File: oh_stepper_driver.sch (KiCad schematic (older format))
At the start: 19 parts, among them P2 CONN_01X02, P3 CONN_01X02, U2 STM32F446RCTx, X1 ABM8G

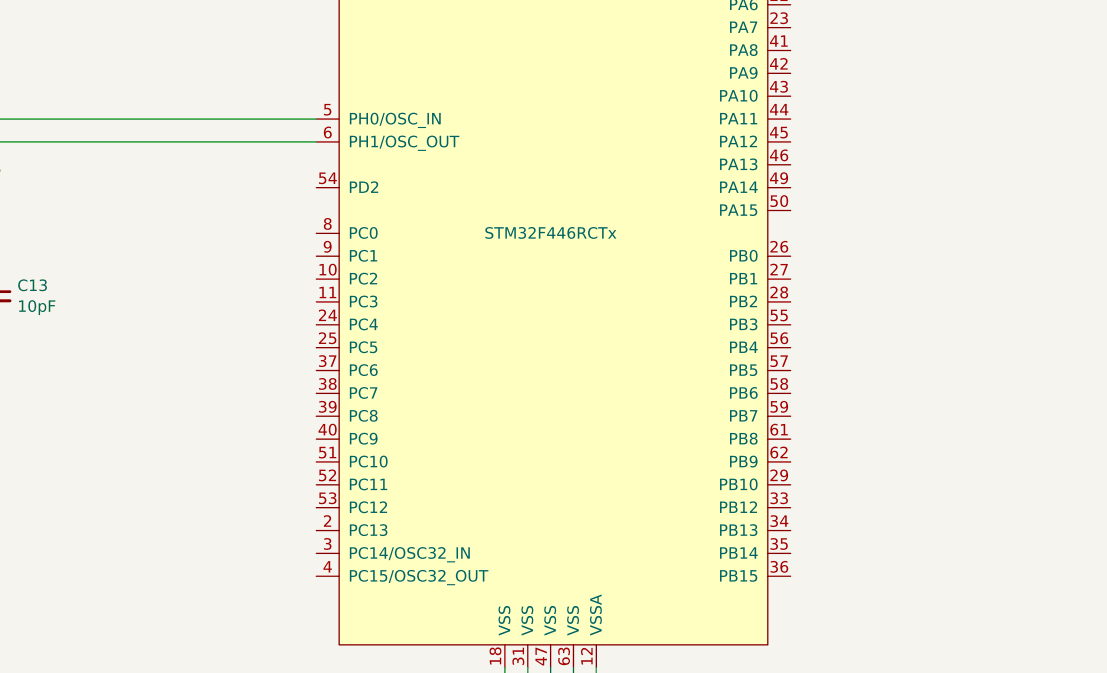
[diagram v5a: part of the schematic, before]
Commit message: connecting control lines between the motor driver and the STM32
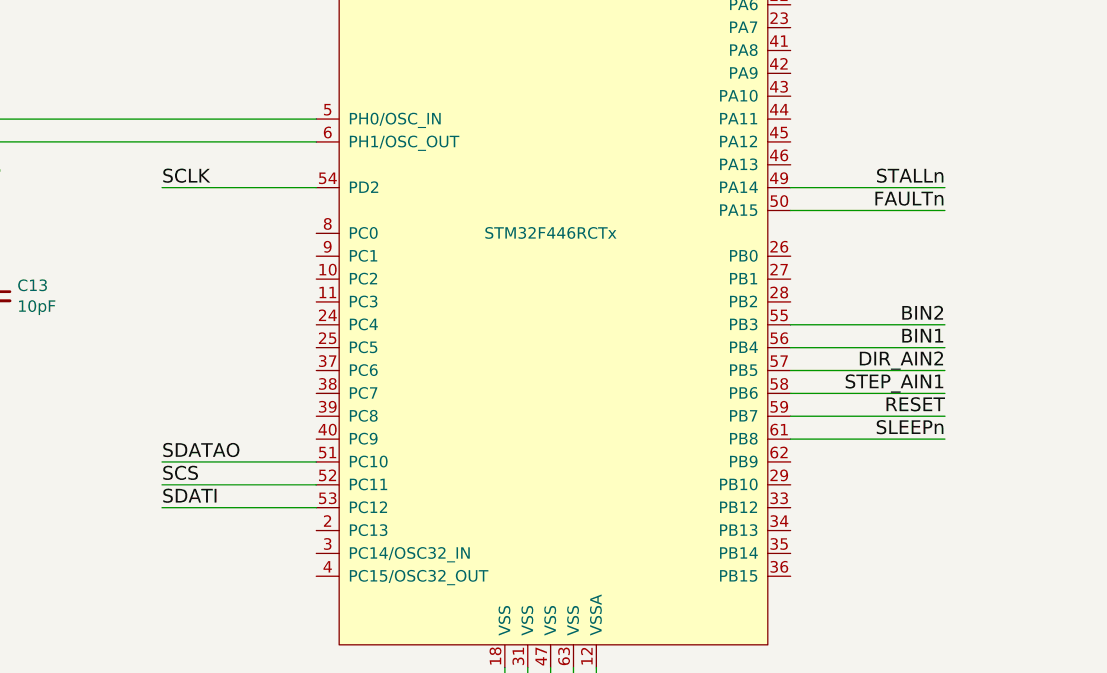
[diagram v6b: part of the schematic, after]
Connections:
- net BIN1: now also U2.56 (PB4)
- net BIN2: now also U2.55 (PB3)
- net DIR_AIN2: now also U2.57 (PB5)
- net FAULTn: now also U2.50 (PA15)
- net RESET: now also U2.59 (PB7)
- net SCLK: now also U2.54 (PD2)
- net SCS: now also U2.52 (PC11)
- net SDATAO: now also U2.51 (PC10)
- net SDATI: now also U2.53 (PC12)
- net SLEEPn: now also U2.61 (PB8)
- net STALLn: now also U2.49 (PA14)
- net STEP_AIN1: now also U2.58 (PB6)
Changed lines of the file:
@@
 $EndDescr
 $Comp
-L GND #PWR4
+L GND #PWR01
 U 1 1 587AE5B3
 P 1400 7200
-F 0 "#PWR4" H 1400 6950 50  0001 C CNN
+F 0 "#PWR01" H 1400 6950 50  0001 C CNN
 F 1 "GND" H 1405 7027 50  0000 C CNN
 F 2 "" H 1400 7200 50  0000 C CNN
@@
 $EndComp
 $Comp
-L VM #PWR3
+L VM #PWR02
 U 1 1 587AE5B4
 P 1400 6950
-F 0 "#PWR3" H 1400 6800 50  0001 C CNN
+F 0 "#PWR02" H 1400 6800 50  0001 C CNN
 F 1 "VM" H 1415 7123 50  0000 C CNN
 F 2 "" H 1400 6950 50  0000 C CNN
@@
 $EndComp
 $Comp
-L GND #PWR6
+L GND #PWR03
 U 1 1 587BB2AD
 P 2400 7200
-F 0 "#PWR6" H 2400 6950 50  0001 C CNN
+F 0 "#PWR03" H 2400 6950 50  0001 C CNN
 F 1 "GND" H 2405 7027 50  0000 C CNN
 F 2 "" H 2400 7200 50  0000 C CNN
@@
 $EndComp
 $Comp
-L VM #PWR5
+L VM #PWR04
 U 1 1 587BB2B3
 P 2400 6950
-F 0 "#PWR5" H 2400 6800 50  0001 C CNN
+F 0 "#PWR04" H 2400 6800 50  0001 C CNN
 F 1 "VM" H 2415 7123 50  0000 C CNN
 F 2 "" H 2400 6950 50  0000 C CNN
@@
 $EndComp
 $Comp
-L GND #PWR8
+L GND #PWR05
 U 1 1 587BC837
 P 3000 7550
-F 0 "#PWR8" H 3000 7300 50  0001 C CNN
+F 0 "#PWR05" H 3000 7300 50  0001 C CNN
 F 1 "GND" H 3005 7377 50  0000 C CNN
 F 2 "" H 3000 7550 50  0000 C CNN
@@
 $EndComp
 $Comp
-L VM #PWR7
+L VM #PWR06
 U 1 1 587BC83D
 P 3000 6850
-F 0 "#PWR7" H 3000 6700 50  0001 C CNN
+F 0 "#PWR06" H 3000 6700 50  0001 C CNN
 F 1 "VM" H 3015 7023 50  0000 C CNN
 F 2 "" H 3000 6850 50  0000 C CNN
@@
 $EndComp
 $Comp
-L GND #PWR1
+L GND #PWR07
 U 1 1 587F36E3
 P 1050 2675
-F 0 "#PWR1" H 1050 2425 50  0001 C CNN
+F 0 "#PWR07" H 1050 2425 50  0001 C CNN
 F 1 "GND" H 1055 2502 50  0000 C CNN
 F 2 "" H 1050 2675 50  0000 C CNN
@@
 $EndComp
 $Comp
-L GND #PWR2
+L GND #PWR08
 U 1 1 587F3A6D
 P 1125 4150
-F 0 "#PWR2" H 1125 3900 50  0001 C CNN
+F 0 "#PWR08" H 1125 3900 50  0001 C CNN
 F 1 "GND" H 1130 3977 50  0000 C CNN
 F 2 "" H 1125 4150 50  0000 C CNN
@@
 $EndComp
 $Comp
-L GND #PWR10
+L GND #PWR09
 U 1 1 587F4021
 P 3800 5675
-F 0 "#PWR10" H 3800 5425 50  0001 C CNN
+F 0 "#PWR09" H 3800 5425 50  0001 C CNN
 F 1 "GND" H 3805 5502 50  0000 C CNN
 F 2 "" H 3800 5675 50  0000 C CNN
@@
 $EndComp
 $Comp
-L +3V3 #PWR9
+L +3V3 #PWR010
 U 1 1 587F4D80
 P 3700 1400
-F 0 "#PWR9" H 3700 1250 50  0001 C CNN
+F 0 "#PWR010" H 3700 1250 50  0001 C CNN
 F 1 "+3V3" H 3715 1573 50  0000 C CNN
 F 2 "" H 3700 1400 50  0000 C CNN
@@
 $EndComp
 $Comp
-L +3V3 #PWR13
+L +3V3 #PWR011
 U 1 1 587F53E0
 P 5375 1250
-F 0 "#PWR13" H 5375 1100 50  0001 C CNN
+F 0 "#PWR011" H 5375 1100 50  0001 C CNN
 F 1 "+3V3" H 5390 1423 50  0000 C CNN
 F 2 "" H 5375 1250 50  0000 C CNN
@@
 $EndComp
 $Comp
-L GND #PWR14
+L GND #PWR012
 U 1 1 587F53FA
 P 5375 1700
-F 0 "#PWR14" H 5375 1450 50  0001 C CNN
+F 0 "#PWR012" H 5375 1450 50  0001 C CNN
 F 1 "GND" H 5380 1527 50  0000 C CNN
 F 2 "" H 5375 1700 50  0000 C CNN
@@
 $EndComp
 $Comp
-L +3.3VADC #PWR15
+L +3.3VADC #PWR013
 U 1 1 587F5AA0
 P 7100 1275
-F 0 "#PWR15" H 7250 1225 50  0001 C CNN
+F 0 "#PWR013" H 7250 1225 50  0001 C CNN
 F 1 "+3.3VADC" H 7120 1418 50  0000 C CNN
 F 2 "" H 7100 1275 50  0000 C CNN
@@
 $EndComp
 $Comp
-L GNDA #PWR16
+L GNDA #PWR014
 U 1 1 587F5ADA
 P 7100 1600
-F 0 "#PWR16" H 7100 1350 50  0001 C CNN
+F 0 "#PWR014" H 7100 1350 50  0001 C CNN
 F 1 "GNDA" H 7105 1427 50  0000 C CNN
 F 2 "" H 7100 1600 50  0000 C CNN
@@
 	7100 1550 7100 1600
 $Comp
-L +3.3VADC #PWR12
+L +3.3VADC #PWR015
 U 1 1 587F5C3A
 P 4100 1375
-F 0 "#PWR12" H 4250 1325 50  0001 C CNN
+F 0 "#PWR015" H 4250 1325 50  0001 C CNN
 F 1 "+3.3VADC" H 4120 1518 50  0000 C CNN
 F 2 "" H 4100 1375 50  0000 C CNN
@@
 Connection ~ 3800 5600
 $Comp
-L GNDA #PWR11
+L GNDA #PWR016
 U 1 1 587F63C7
 P 4050 5675
-F 0 "#PWR11" H 4050 5425 50  0001 C CNN
+F 0 "#PWR016" H 4050 5425 50  0001 C CNN
 F 1 "GNDA" H 4055 5502 50  0000 C CNN
 F 2 "" H 4050 5675 50  0000 C CNN
@@
 Text Label 7450 3100 0    60   ~ 0
 RESET
+Wire Wire Line
+	4900 4500 5575 4500
+Text Label 5575 4500 2    60   ~ 0
+SLEEPn
+Wire Wire Line
+	4900 4400 5575 4400
+Wire Wire Line
+	4900 4300 5575 4300
+Text Label 5575 4300 2    60   ~ 0
+STEP_AIN1
+Wire Wire Line
+	4900 4200 5575 4200
+Wire Wire Line
+	4900 4100 5575 4100
+Text Label 5575 4100 2    60   ~ 0
+BIN1
+Wire Wire Line
+	4900 4000 5575 4000
+Wire Wire Line
+	2825 3400 2150 3400
+Text Label 2150 3400 0    60   ~ 0
+SCLK
+Wire Wire Line
+	2825 4800 2150 4800
+Wire Wire Line
+	2825 4700 2150 4700
+Text Label 2150 4700 0    60   ~ 0
+SCS
+Wire Wire Line
+	2825 4600 2150 4600
+Wire Wire Line
+	4900 3500 5575 3500
+Text Label 5575 3500 2    60   ~ 0
+FAULTn
+Wire Wire Line
+	4900 3400 5575 3400
+Text Label 5575 3400 2    60   ~ 0
+STALLn
+Text Label 2150 4600 0    60   ~ 0
+SDATAO
+Text Label 2150 4800 0    60   ~ 0
+SDATI
+Text Label 5575 4000 2    60   ~ 0
+BIN2
+Text Label 5575 4200 2    60   ~ 0
+DIR_AIN2
+Text Label 5575 4400 2    60   ~ 0
+RESET
 $EndSCHEMATC

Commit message: connecting mcu
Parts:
- added L1: FB, Resistors_SMD:R_0603, symbol L_Small
- added SW1: BOOT_MODE, symbol SWITCH_INV
- added SW2: RST, symbol SW_PUSH
- R13: value 47k -> 10k
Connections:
- net +3.3VADC: now also L1.2
- net +3V3: now also U2.1 (VBAT), L1.1, SW1.3
- net BIN1: now also U2.41 (PA8); no longer U2.56 (PB4)
- net BIN2: now also U2.23 (PA7); no longer U2.55 (PB3)
- net DIR_AIN2: now also U2.42 (PA9); no longer U2.57 (PB5)
- net FAULTn: now also U2.22 (PA6); no longer U2.50 (PA15)
- net GND: now also SW1.1, SW2.2; no longer R13.2
- net RESET: now also U2.44 (PA11); no longer U2.59 (PB7)
- net SLEEPn: now also U2.45 (PA12); no longer U2.61 (PB8)
- net STALLn: now also U2.21 (PA5); no longer U2.49 (PA14)
- net STEP_AIN1: now also U2.43 (PA10); no longer U2.58 (PB6)
- net JTMS: now reaches U2.46 (PA13)
- net at C11.1, U2.7 (NRST): now also SW2.1
- new net: R13.2, SW1.2
- new net JTCK: U2.49 (PA14)
- new net JTDI: U2.50 (PA15)
- new net JTDO: U2.55 (PB3)
- new net NJTRST: U2.56 (PB4)
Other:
- note added: "600 Ohm @100MHz \ni.e: 742792653"
- moved on the sheet: C11, C12, C14, R13

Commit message: fp-lib-table fixed
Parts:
- X1: footprint SMD:ASDMB -> (none)
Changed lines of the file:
@@
 EESchema Schematic File Version 2
+LIBS:csd18531q5a
+LIBS:drv8711
+LIBS:stm32f446_lqfp64
+LIBS:abm8g
 LIBS:oh_stepper_driver-rescue
 LIBS:power
@@
 LIBS:contrib
 LIBS:valves
-LIBS:csd18531q5a
-LIBS:drv8711
-LIBS:stm32f446_lqfp64
-LIBS:abm8g
 LIBS:oh_stepper_driver-cache
 EELAYER 26 0
@@
 F 0 "C6" H 3115 7196 50  0000 L CNN
 F 1 "100uF" H 3115 7105 50  0000 L CNN
-F 2 "" H 3000 7150 50  0000 C CNN
+F 2 "" H 3000 7150 50  0001 C CNN
 F 3 "" H 3000 7150 50  0000 C CNN
 	1    3000 7150
@@
 F 0 "X1" H 1050 3500 60  0000 C CNN
 F 1 "ABM8G" H 1125 3175 60  0000 C CNN
-F 2 "SMD:ASDMB" H 1125 3325 60  0001 C CNN
+F 2 "" H 1125 3325 60  0001 C CNN
 F 3 "" H 1125 3325 60  0001 C CNN
 	1    1125 3325
@@
 F 0 "SW1" H 1225 1885 50  0000 C CNN
 F 1 "BOOT_MODE" H 1225 1976 50  0000 C CNN
-F 2 "" H 1225 2200 50  0000 C CNN
+F 2 "" H 1225 2200 50  0001 C CNN
 F 3 "" H 1225 2200 50  0000 C CNN
 	1    1225 2200
@@
 F 0 "SW2" V 2079 1518 50  0000 L CNN
 F 1 "RST" V 2170 1518 50  0000 L CNN
-F 2 "" H 2125 1400 50  0000 C CNN
+F 2 "" H 2125 1400 50  0001 C CNN
 F 3 "" H 2125 1400 50  0000 C CNN
 	1    2125 1400
